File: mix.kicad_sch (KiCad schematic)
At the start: 6 parts

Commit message: started to work on power part
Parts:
- gave numbers to parts that had none: 4
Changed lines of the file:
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@@
   (symbol (lib_id "eurorack:R-10k-1206") (at 88.265 76.835 90) (unit 1)
     (in_bom yes) (on_board yes) (fields_autoplaced)
-    (property "Reference" "R?" (id 0) (at 88.265 71.12 90))
+    (property "Reference" "R32" (id 0) (at 88.265 71.12 90))
     (property "Value" "R-10k-1206" (id 1) (at 88.265 73.66 90))
     (property "Footprint" "Resistor_SMD:R_1206_3216Metric_Pad1.30x1.75mm_HandSolder" (id 2) (at 88.265 78.613 90)
@@
   (symbol (lib_id "eurorack:TL072") (at 109.855 107.315 0) (mirror x) (unit 2)
     (in_bom yes) (on_board yes) (fields_autoplaced)
-    (property "Reference" "U?" (id 0) (at 109.855 118.11 0))
+    (property "Reference" "U6" (id 0) (at 109.855 118.11 0))
     (property "Value" "TL072" (id 1) (at 109.855 115.57 0))
     (property "Footprint" "Package_SO:SO-8_3.9x4.9mm_P1.27mm" (id 2) (at 109.855 107.315 0)
@@
   (symbol (lib_id "eurorack:R-10k-1206") (at 110.49 63.5 90) (unit 1)
     (in_bom yes) (on_board yes) (fields_autoplaced)
-    (property "Reference" "R?" (id 0) (at 110.49 57.15 90))
+    (property "Reference" "R33" (id 0) (at 110.49 57.15 90))
     (property "Value" "R-10k-1206" (id 1) (at 110.49 59.69 90))
     (property "Footprint" "Resistor_SMD:R_1206_3216Metric_Pad1.30x1.75mm_HandSolder" (id 2) (at 110.49 65.278 90)
@@
   (symbol (lib_id "eurorack:TL072") (at 109.855 79.375 0) (mirror x) (unit 1)
     (in_bom yes) (on_board yes) (fields_autoplaced)
-    (property "Reference" "U?" (id 0) (at 109.855 68.58 0))
+    (property "Reference" "U6" (id 0) (at 109.855 68.58 0))
     (property "Value" "TL072" (id 1) (at 109.855 71.12 0))
     (property "Footprint" "Package_SO:SO-8_3.9x4.9mm_P1.27mm" (id 2) (at 109.855 79.375 0)
@@
   (symbol (lib_id "power:+12V") (at 199.39 24.765 0) (unit 1)
     (in_bom yes) (on_board yes) (fields_autoplaced)
-    (property "Reference" "#PWR?" (id 0) (at 199.39 28.575 0)
+    (property "Reference" "#PWR051" (id 0) (at 199.39 28.575 0)
       (effects (font (size 1.27 1.27)) hide)
     )
@@
   (symbol (lib_id "power:-12V") (at 199.39 42.545 180) (unit 1)
     (in_bom yes) (on_board yes) (fields_autoplaced)
-    (property "Reference" "#PWR?" (id 0) (at 199.39 45.085 0)
+    (property "Reference" "#PWR052" (id 0) (at 199.39 45.085 0)
       (effects (font (size 1.27 1.27)) hide)
     )
@@
   (symbol (lib_id "eurorack:R-10k-1206") (at 88.265 67.31 90) (unit 1)
     (in_bom yes) (on_board yes) (fields_autoplaced)
-    (property "Reference" "R?" (id 0) (at 88.265 60.96 90))
+    (property "Reference" "R31" (id 0) (at 88.265 60.96 90))
     (property "Value" "R-10k-1206" (id 1) (at 88.265 63.5 90))
     (property "Footprint" "Resistor_SMD:R_1206_3216Metric_Pad1.30x1.75mm_HandSolder" (id 2) (at 88.265 69.088 90)
@@
   (symbol (lib_id "power:GND") (at 97.155 109.855 0) (mirror y) (unit 1)
     (in_bom yes) (on_board yes) (fields_autoplaced)
-    (property "Reference" "#PWR?" (id 0) (at 97.155 116.205 0)
+    (property "Reference" "#PWR049" (id 0) (at 97.155 116.205 0)
       (effects (font (size 1.27 1.27)) hide)
     )
@@
   (symbol (lib_id "power:GND") (at 99.695 85.09 0) (unit 1)
     (in_bom yes) (on_board yes) (fields_autoplaced)
-    (property "Reference" "#PWR?" (id 0) (at 99.695 91.44 0)
+    (property "Reference" "#PWR050" (id 0) (at 99.695 91.44 0)
       (effects (font (size 1.27 1.27)) hide)
     )
@@
   (symbol (lib_id "eurorack:TL072") (at 201.93 33.655 0) (unit 3)
     (in_bom yes) (on_board yes) (fields_autoplaced)
-    (property "Reference" "U?" (id 0) (at 200.66 32.3849 0)
+    (property "Reference" "U6" (id 0) (at 200.66 32.3849 0)
       (effects (font (size 1.27 1.27)) (justify left))
     )

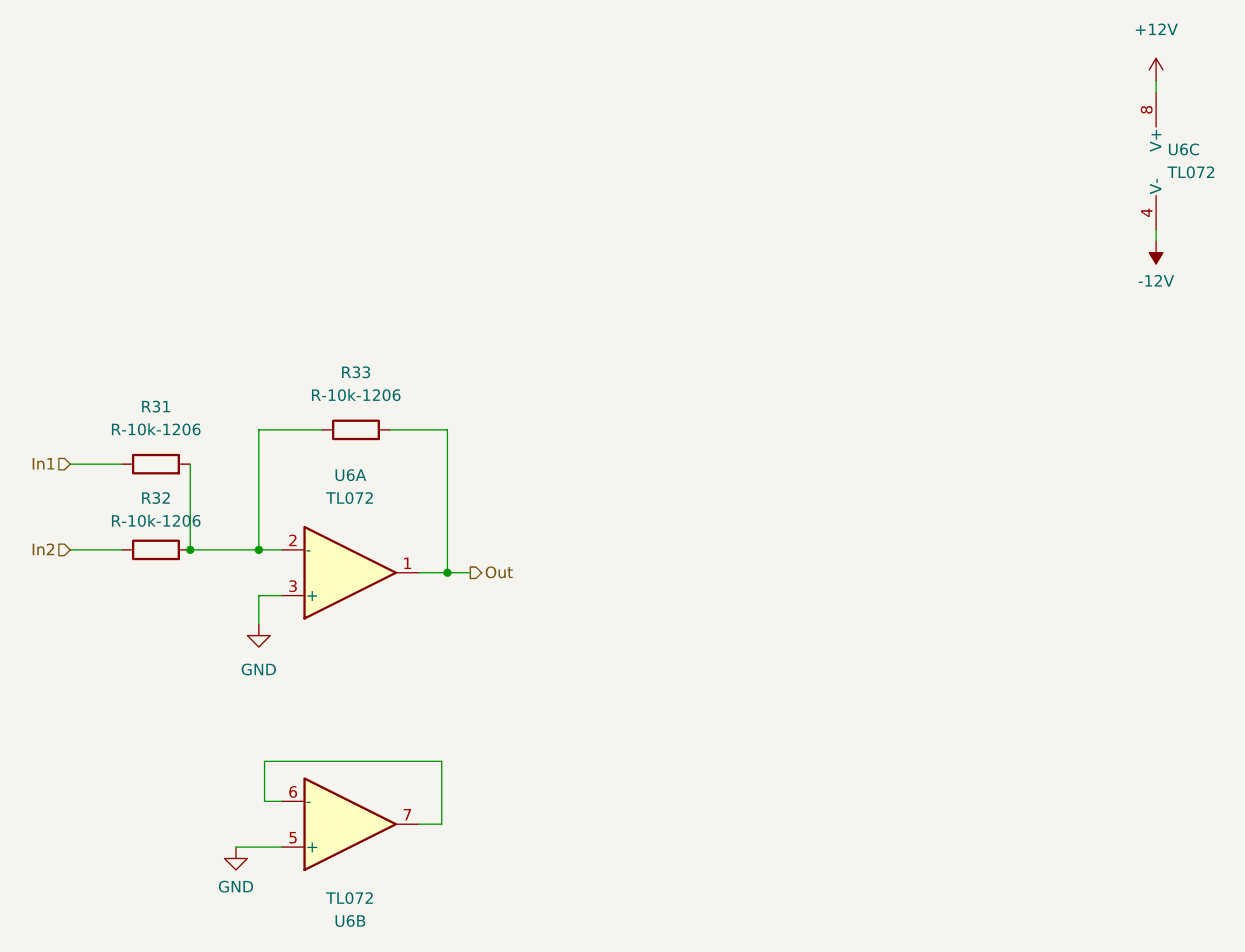
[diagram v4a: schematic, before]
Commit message: refactoring with global labels
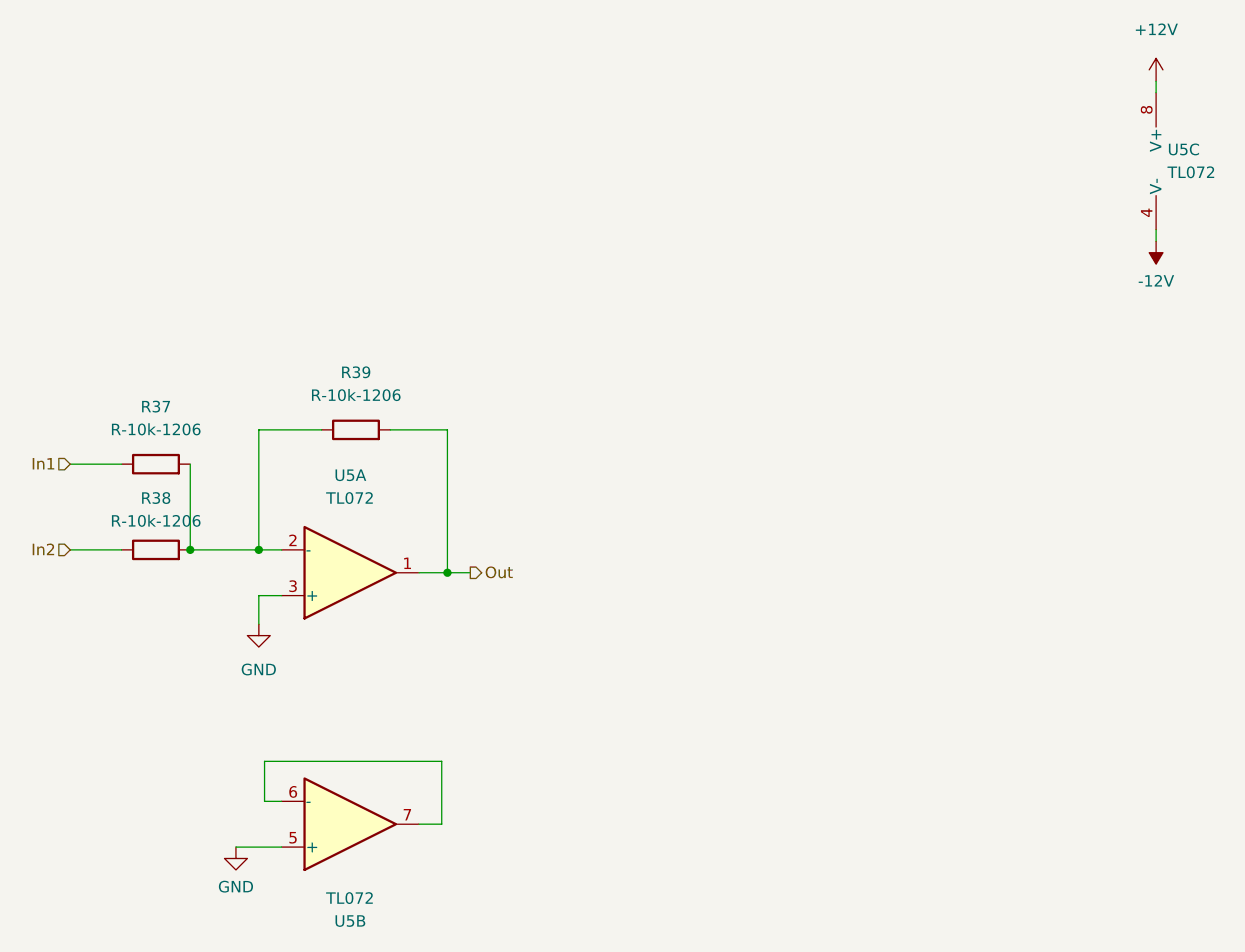
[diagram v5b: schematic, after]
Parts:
- renumbered R31 to R37, R32 to R38, R33 to R39, U6 to U5
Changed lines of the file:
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@@
   (symbol (lib_id "eurorack:R-10k-1206") (at 88.265 76.835 90) (unit 1)
     (in_bom yes) (on_board yes) (fields_autoplaced)
-    (property "Reference" "R32" (id 0) (at 88.265 71.12 90))
+    (property "Reference" "R38" (id 0) (at 88.265 71.12 90))
     (property "Value" "R-10k-1206" (id 1) (at 88.265 73.66 90))
     (property "Footprint" "Resistor_SMD:R_1206_3216Metric_Pad1.30x1.75mm_HandSolder" (id 2) (at 88.265 78.613 90)
@@
   (symbol (lib_id "eurorack:TL072") (at 109.855 107.315 0) (mirror x) (unit 2)
     (in_bom yes) (on_board yes) (fields_autoplaced)
-    (property "Reference" "U6" (id 0) (at 109.855 118.11 0))
+    (property "Reference" "U5" (id 0) (at 109.855 118.11 0))
     (property "Value" "TL072" (id 1) (at 109.855 115.57 0))
     (property "Footprint" "Package_SO:SO-8_3.9x4.9mm_P1.27mm" (id 2) (at 109.855 107.315 0)
@@
   (symbol (lib_id "eurorack:R-10k-1206") (at 110.49 63.5 90) (unit 1)
     (in_bom yes) (on_board yes) (fields_autoplaced)
-    (property "Reference" "R33" (id 0) (at 110.49 57.15 90))
+    (property "Reference" "R39" (id 0) (at 110.49 57.15 90))
     (property "Value" "R-10k-1206" (id 1) (at 110.49 59.69 90))
     (property "Footprint" "Resistor_SMD:R_1206_3216Metric_Pad1.30x1.75mm_HandSolder" (id 2) (at 110.49 65.278 90)
@@
   (symbol (lib_id "eurorack:TL072") (at 109.855 79.375 0) (mirror x) (unit 1)
     (in_bom yes) (on_board yes) (fields_autoplaced)
-    (property "Reference" "U6" (id 0) (at 109.855 68.58 0))
+    (property "Reference" "U5" (id 0) (at 109.855 68.58 0))
     (property "Value" "TL072" (id 1) (at 109.855 71.12 0))
     (property "Footprint" "Package_SO:SO-8_3.9x4.9mm_P1.27mm" (id 2) (at 109.855 79.375 0)
@@
   (symbol (lib_id "power:+12V") (at 199.39 24.765 0) (unit 1)
     (in_bom yes) (on_board yes) (fields_autoplaced)
-    (property "Reference" "#PWR051" (id 0) (at 199.39 28.575 0)
+    (property "Reference" "#PWR057" (id 0) (at 199.39 28.575 0)
       (effects (font (size 1.27 1.27)) hide)
     )
@@
   (symbol (lib_id "power:-12V") (at 199.39 42.545 180) (unit 1)
     (in_bom yes) (on_board yes) (fields_autoplaced)
-    (property "Reference" "#PWR052" (id 0) (at 199.39 45.085 0)
+    (property "Reference" "#PWR058" (id 0) (at 199.39 45.085 0)
       (effects (font (size 1.27 1.27)) hide)
     )
@@
   (symbol (lib_id "eurorack:R-10k-1206") (at 88.265 67.31 90) (unit 1)
     (in_bom yes) (on_board yes) (fields_autoplaced)
-    (property "Reference" "R31" (id 0) (at 88.265 60.96 90))
+    (property "Reference" "R37" (id 0) (at 88.265 60.96 90))
     (property "Value" "R-10k-1206" (id 1) (at 88.265 63.5 90))
     (property "Footprint" "Resistor_SMD:R_1206_3216Metric_Pad1.30x1.75mm_HandSolder" (id 2) (at 88.265 69.088 90)
@@
   (symbol (lib_id "power:GND") (at 97.155 109.855 0) (mirror y) (unit 1)
     (in_bom yes) (on_board yes) (fields_autoplaced)
-    (property "Reference" "#PWR049" (id 0) (at 97.155 116.205 0)
+    (property "Reference" "#PWR055" (id 0) (at 97.155 116.205 0)
       (effects (font (size 1.27 1.27)) hide)
     )
@@
   (symbol (lib_id "power:GND") (at 99.695 85.09 0) (unit 1)
     (in_bom yes) (on_board yes) (fields_autoplaced)
-    (property "Reference" "#PWR050" (id 0) (at 99.695 91.44 0)
+    (property "Reference" "#PWR056" (id 0) (at 99.695 91.44 0)
       (effects (font (size 1.27 1.27)) hide)
     )
@@
   (symbol (lib_id "eurorack:TL072") (at 201.93 33.655 0) (unit 3)
     (in_bom yes) (on_board yes) (fields_autoplaced)
-    (property "Reference" "U6" (id 0) (at 200.66 32.3849 0)
+    (property "Reference" "U5" (id 0) (at 200.66 32.3849 0)
       (effects (font (size 1.27 1.27)) (justify left))
     )

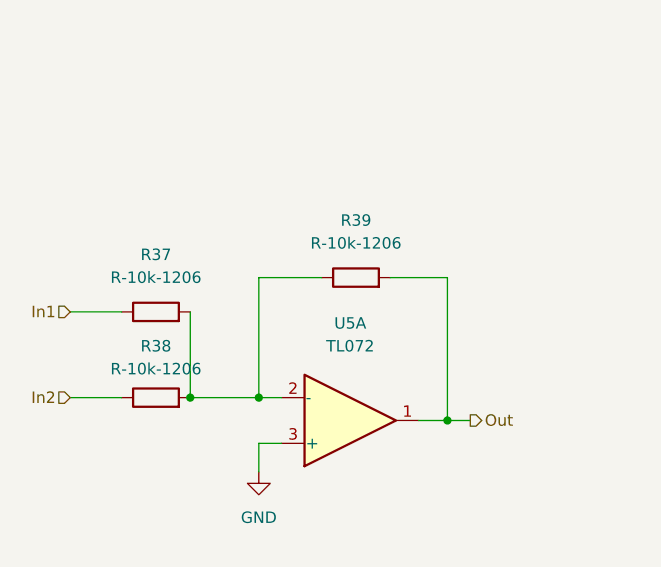
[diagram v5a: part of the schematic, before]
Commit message: cleaning into modules
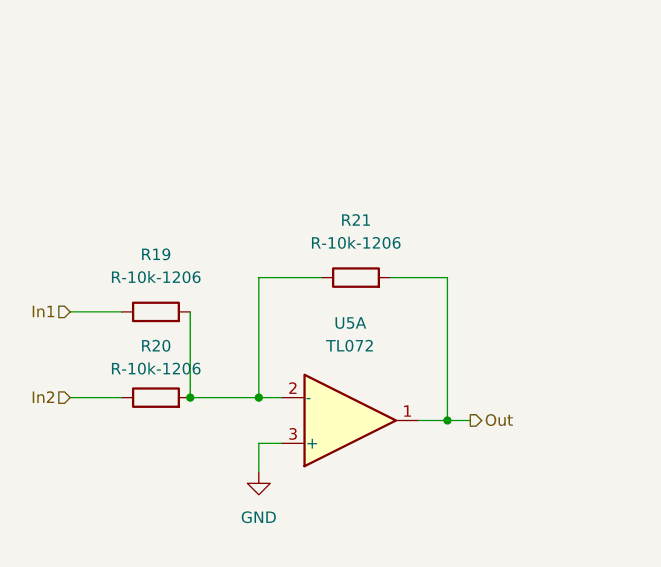
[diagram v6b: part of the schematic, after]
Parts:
- renumbered R37 to R19, R38 to R20, R39 to R21
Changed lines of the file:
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@@
   (symbol (lib_id "eurorack:R-10k-1206") (at 88.265 76.835 90) (unit 1)
     (in_bom yes) (on_board yes) (fields_autoplaced)
-    (property "Reference" "R38" (id 0) (at 88.265 71.12 90))
+    (property "Reference" "R20" (id 0) (at 88.265 71.12 90))
     (property "Value" "R-10k-1206" (id 1) (at 88.265 73.66 90))
     (property "Footprint" "Resistor_SMD:R_1206_3216Metric_Pad1.30x1.75mm_HandSolder" (id 2) (at 88.265 78.613 90)
@@
       (effects (font (size 1.27 1.27)) hide)
     )
-    (pin "1")
-    (pin "2")
-    (pin "3")
     (pin "5")
     (pin "6")
     (pin "7")
-    (pin "4")
-    (pin "8")
   )
   (symbol (lib_id "eurorack:R-10k-1206") (at 110.49 63.5 90) (unit 1)
     (in_bom yes) (on_board yes) (fields_autoplaced)
-    (property "Reference" "R39" (id 0) (at 110.49 57.15 90))
+    (property "Reference" "R21" (id 0) (at 110.49 57.15 90))
     (property "Value" "R-10k-1206" (id 1) (at 110.49 59.69 90))
     (property "Footprint" "Resistor_SMD:R_1206_3216Metric_Pad1.30x1.75mm_HandSolder" (id 2) (at 110.49 65.278 90)
@@
     (pin "2")
     (pin "3")
-    (pin "5")
-    (pin "6")
-    (pin "7")
-    (pin "4")
-    (pin "8")
   )
   (symbol (lib_id "power:+12V") (at 199.39 24.765 0) (unit 1)
     (in_bom yes) (on_board yes) (fields_autoplaced)
-    (property "Reference" "#PWR057" (id 0) (at 199.39 28.575 0)
+    (property "Reference" "#PWR054" (id 0) (at 199.39 28.575 0)
       (effects (font (size 1.27 1.27)) hide)
     )
@@
   (symbol (lib_id "power:-12V") (at 199.39 42.545 180) (unit 1)
     (in_bom yes) (on_board yes) (fields_autoplaced)
-    (property "Reference" "#PWR058" (id 0) (at 199.39 45.085 0)
+    (property "Reference" "#PWR055" (id 0) (at 199.39 45.085 0)
       (effects (font (size 1.27 1.27)) hide)
     )
@@
   (symbol (lib_id "eurorack:R-10k-1206") (at 88.265 67.31 90) (unit 1)
     (in_bom yes) (on_board yes) (fields_autoplaced)
-    (property "Reference" "R37" (id 0) (at 88.265 60.96 90))
+    (property "Reference" "R19" (id 0) (at 88.265 60.96 90))
     (property "Value" "R-10k-1206" (id 1) (at 88.265 63.5 90))
     (property "Footprint" "Resistor_SMD:R_1206_3216Metric_Pad1.30x1.75mm_HandSolder" (id 2) (at 88.265 69.088 90)
@@
   (symbol (lib_id "power:GND") (at 97.155 109.855 0) (mirror y) (unit 1)
     (in_bom yes) (on_board yes) (fields_autoplaced)
-    (property "Reference" "#PWR055" (id 0) (at 97.155 116.205 0)
+    (property "Reference" "#PWR052" (id 0) (at 97.155 116.205 0)
       (effects (font (size 1.27 1.27)) hide)
     )
@@
   (symbol (lib_id "power:GND") (at 99.695 85.09 0) (unit 1)
     (in_bom yes) (on_board yes) (fields_autoplaced)
-    (property "Reference" "#PWR056" (id 0) (at 99.695 91.44 0)
+    (property "Reference" "#PWR053" (id 0) (at 99.695 91.44 0)
       (effects (font (size 1.27 1.27)) hide)
     )
@@
       (effects (font (size 1.27 1.27)) hide)
     )
-    (pin "1")
-    (pin "2")
-    (pin "3")
-    (pin "5")
-    (pin "6")
-    (pin "7")
     (pin "4")
     (pin "8")

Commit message: working on AD inputs
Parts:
- renumbered R19 to R33, R20 to R34, R21 to R35, U5 to U19
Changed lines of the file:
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@@
   (symbol (lib_id "eurorack:R-10k-1206") (at 88.265 76.835 90) (unit 1)
     (in_bom yes) (on_board yes) (fields_autoplaced)
-    (property "Reference" "R20" (id 0) (at 88.265 71.12 90))
+    (property "Reference" "R34" (id 0) (at 88.265 71.12 90))
     (property "Value" "R-10k-1206" (id 1) (at 88.265 73.66 90))
     (property "Footprint" "Resistor_SMD:R_1206_3216Metric_Pad1.30x1.75mm_HandSolder" (id 2) (at 88.265 78.613 90)
@@
   (symbol (lib_id "eurorack:TL072") (at 109.855 107.315 0) (mirror x) (unit 2)
     (in_bom yes) (on_board yes) (fields_autoplaced)
-    (property "Reference" "U5" (id 0) (at 109.855 118.11 0))
+    (property "Reference" "U19" (id 0) (at 109.855 118.11 0))
     (property "Value" "TL072" (id 1) (at 109.855 115.57 0))
     (property "Footprint" "Package_SO:SO-8_3.9x4.9mm_P1.27mm" (id 2) (at 109.855 107.315 0)
@@
   (symbol (lib_id "eurorack:R-10k-1206") (at 110.49 63.5 90) (unit 1)
     (in_bom yes) (on_board yes) (fields_autoplaced)
-    (property "Reference" "R21" (id 0) (at 110.49 57.15 90))
+    (property "Reference" "R35" (id 0) (at 110.49 57.15 90))
     (property "Value" "R-10k-1206" (id 1) (at 110.49 59.69 90))
     (property "Footprint" "Resistor_SMD:R_1206_3216Metric_Pad1.30x1.75mm_HandSolder" (id 2) (at 110.49 65.278 90)
@@
   (symbol (lib_id "eurorack:TL072") (at 109.855 79.375 0) (mirror x) (unit 1)
     (in_bom yes) (on_board yes) (fields_autoplaced)
-    (property "Reference" "U5" (id 0) (at 109.855 68.58 0))
+    (property "Reference" "U19" (id 0) (at 109.855 68.58 0))
     (property "Value" "TL072" (id 1) (at 109.855 71.12 0))
     (property "Footprint" "Package_SO:SO-8_3.9x4.9mm_P1.27mm" (id 2) (at 109.855 79.375 0)
@@
   (symbol (lib_id "power:+12V") (at 199.39 24.765 0) (unit 1)
     (in_bom yes) (on_board yes) (fields_autoplaced)
-    (property "Reference" "#PWR055" (id 0) (at 199.39 28.575 0)
+    (property "Reference" "#PWR090" (id 0) (at 199.39 28.575 0)
       (effects (font (size 1.27 1.27)) hide)
     )
@@
   (symbol (lib_id "power:-12V") (at 199.39 42.545 180) (unit 1)
     (in_bom yes) (on_board yes) (fields_autoplaced)
-    (property "Reference" "#PWR056" (id 0) (at 199.39 45.085 0)
+    (property "Reference" "#PWR091" (id 0) (at 199.39 45.085 0)
       (effects (font (size 1.27 1.27)) hide)
     )
@@
   (symbol (lib_id "eurorack:R-10k-1206") (at 88.265 67.31 90) (unit 1)
     (in_bom yes) (on_board yes) (fields_autoplaced)
-    (property "Reference" "R19" (id 0) (at 88.265 60.96 90))
+    (property "Reference" "R33" (id 0) (at 88.265 60.96 90))
     (property "Value" "R-10k-1206" (id 1) (at 88.265 63.5 90))
     (property "Footprint" "Resistor_SMD:R_1206_3216Metric_Pad1.30x1.75mm_HandSolder" (id 2) (at 88.265 69.088 90)
@@
   (symbol (lib_id "power:GND") (at 97.155 109.855 0) (mirror y) (unit 1)
     (in_bom yes) (on_board yes) (fields_autoplaced)
-    (property "Reference" "#PWR053" (id 0) (at 97.155 116.205 0)
+    (property "Reference" "#PWR088" (id 0) (at 97.155 116.205 0)
       (effects (font (size 1.27 1.27)) hide)
     )
@@
   (symbol (lib_id "power:GND") (at 99.695 85.09 0) (unit 1)
     (in_bom yes) (on_board yes) (fields_autoplaced)
-    (property "Reference" "#PWR054" (id 0) (at 99.695 91.44 0)
+    (property "Reference" "#PWR089" (id 0) (at 99.695 91.44 0)
       (effects (font (size 1.27 1.27)) hide)
     )
@@
   (symbol (lib_id "eurorack:TL072") (at 201.93 33.655 0) (unit 3)
     (in_bom yes) (on_board yes) (fields_autoplaced)
-    (property "Reference" "U5" (id 0) (at 200.66 32.3849 0)
+    (property "Reference" "U19" (id 0) (at 200.66 32.3849 0)
       (effects (font (size 1.27 1.27)) (justify left))
     )
